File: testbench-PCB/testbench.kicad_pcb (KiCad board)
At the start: 2 copper layers, 185.4 x 134.6 mm, 67 parts, among them J1 USB_C_Receptacle_USB2.0, J2 AVR-ISP, J3 AVR-JTAG, SW1 SW_Push, U1 ATmega2561-16A, U10 CH340C, U2 Thermistor_module, U3 Rotary_encoder_switch_module, U4 RTC_EEPROM_module, U6 Relay_module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

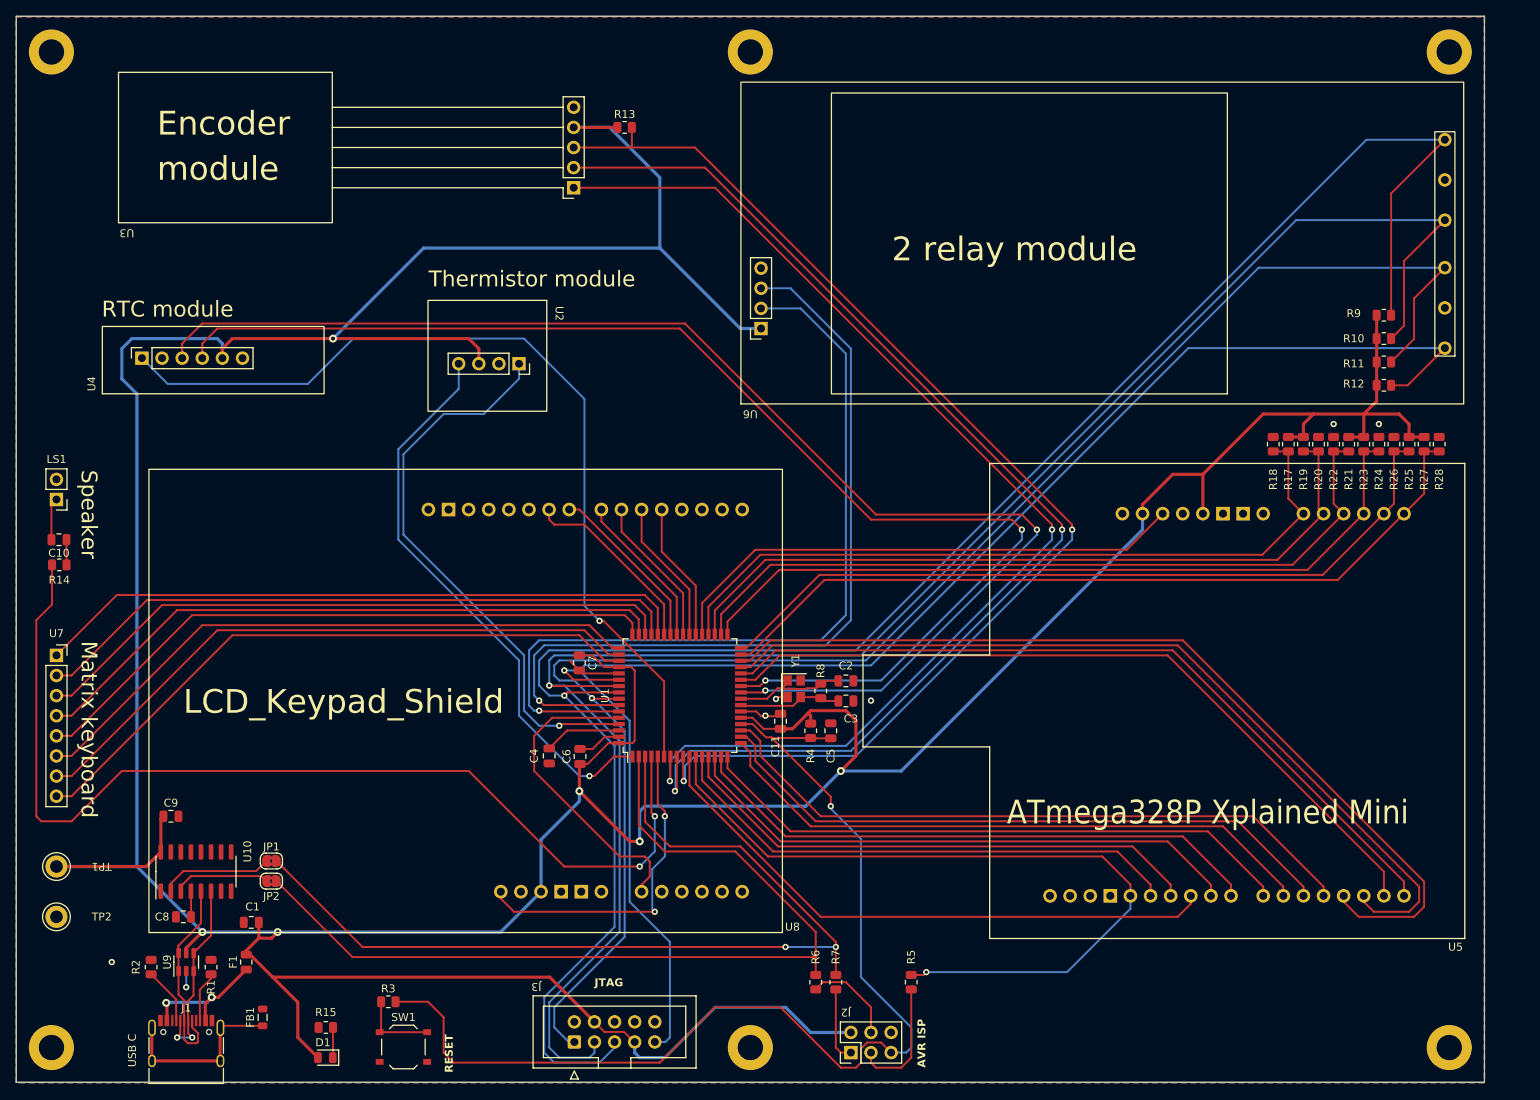
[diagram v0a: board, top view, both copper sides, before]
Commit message: Changed encoder module pinout, added labels.
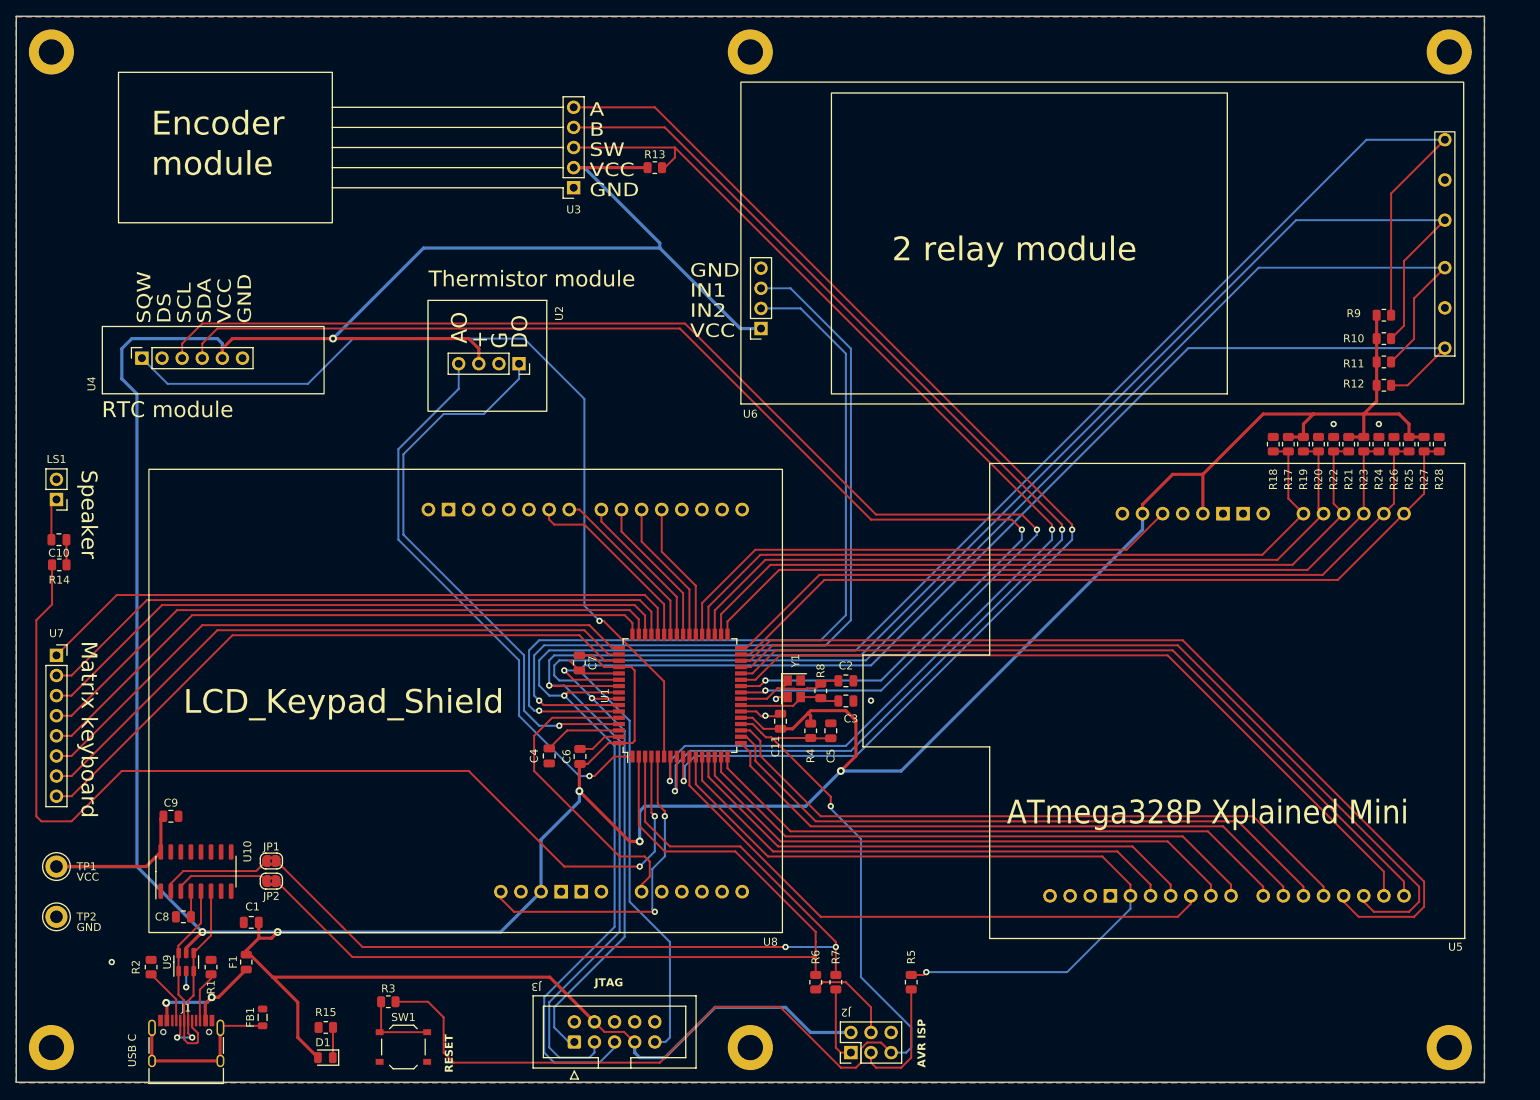
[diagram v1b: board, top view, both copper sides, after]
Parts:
- moved R13 6.35 mm to (118.7, 46.4)
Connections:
- U1 pad 7: /Kit modules/ENC.A -> /Kit modules/ENC.SW
- U1 pad 9: /Kit modules/ENC.SW -> /Kit modules/ENC.A
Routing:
- net /Kit modules/ENC.A: track 145.4 -> 152.5 mm
- net +5V: track 638.7 -> 635.6 mm
- net /Kit modules/ENC.B: track 150.6 -> 152.7 mm
- net /Kit modules/ENC.SW: track 153.1 -> 151.0 mm
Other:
- board text added: "+"
- board text added: "A"
- board text added: "AO"
- board text added: "B"
- board text added: "DO"
- board text added: "DS"
- board text added: "G"
- board text added: "GND"
- board text added: "IN1"
- board text added: "IN2"
- board text added: "SCL"
- board text added: "SDA"
- board text added: "SQW"
- board text added: "SW"
- board text added: "VCC"

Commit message: Added protective resistors.
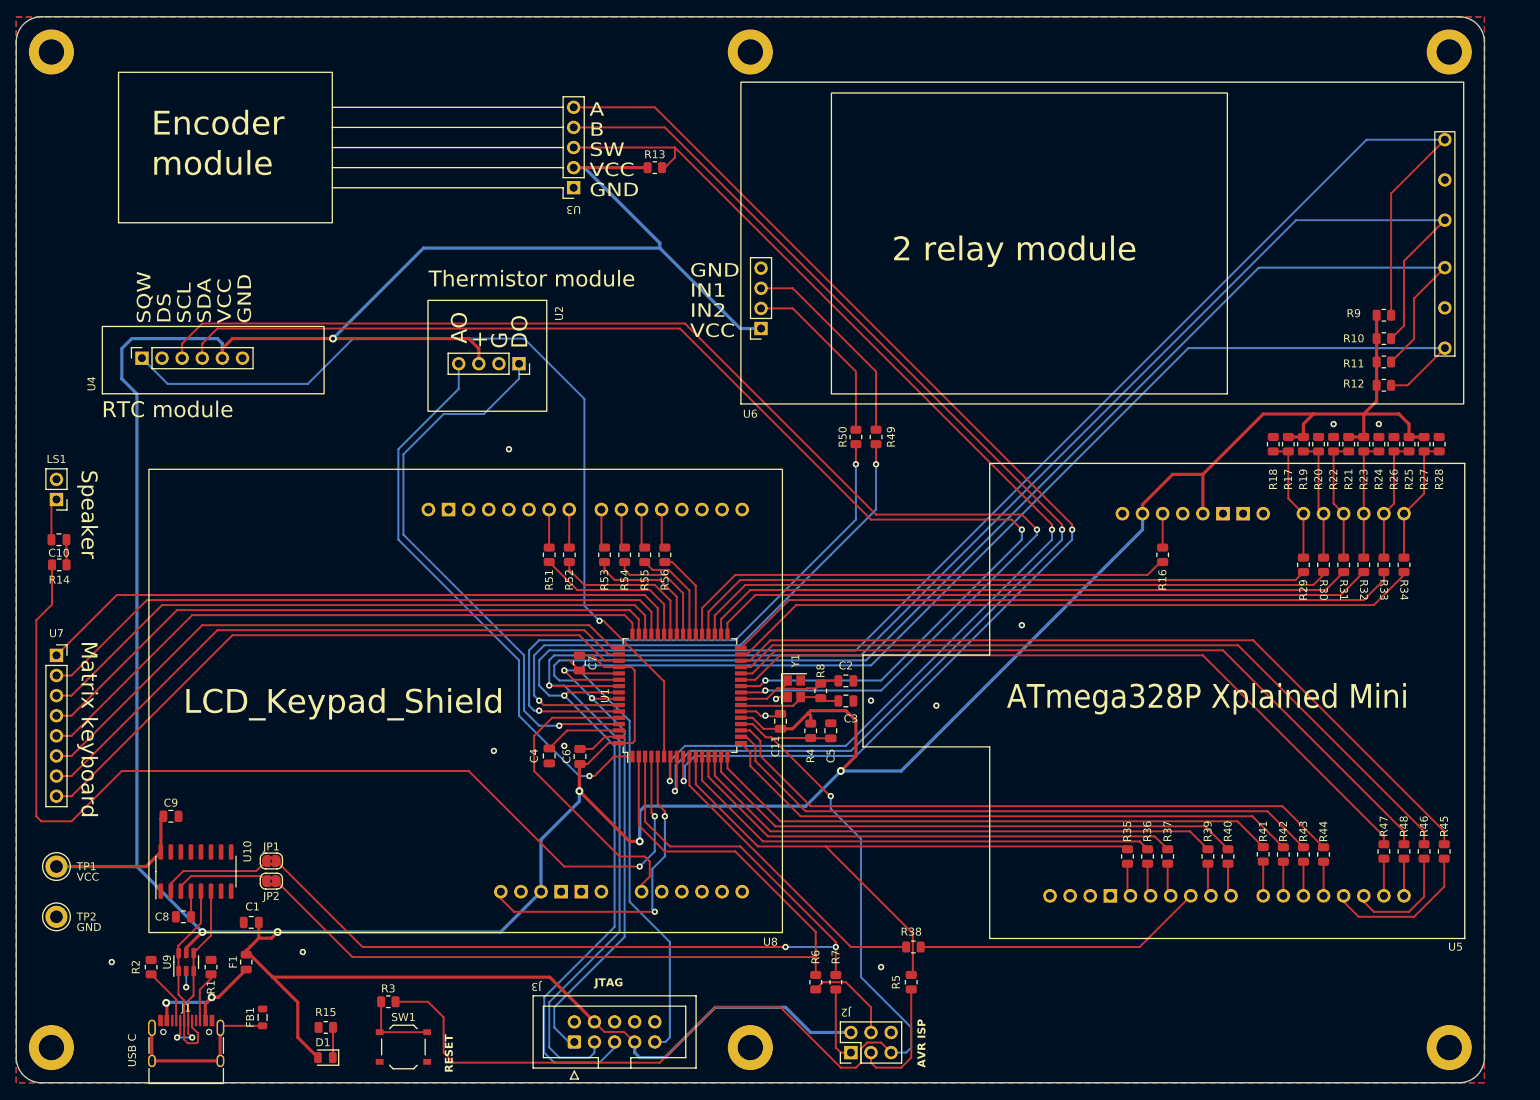
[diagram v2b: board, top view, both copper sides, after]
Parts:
- added R16: 330R, Resistor_SMD:R_0805_2012Metric, F.Cu at (182.9, 95.2)
- added R29: 330R, Resistor_SMD:R_0805_2012Metric, F.Cu at (200.7, 96.5)
- added R30: 330R, Resistor_SMD:R_0805_2012Metric, F.Cu at (203.2, 96.5)
- added R31: 330R, Resistor_SMD:R_0805_2012Metric, F.Cu at (205.7, 96.5)
- added R32: 330R, Resistor_SMD:R_0805_2012Metric, F.Cu at (208.3, 96.5)
- added R33: 330R, Resistor_SMD:R_0805_2012Metric, F.Cu at (210.8, 96.5)
- added R34: 330R, Resistor_SMD:R_0805_2012Metric, F.Cu at (213.4, 96.5)
- added R35: 330R, Resistor_SMD:R_0805_2012Metric, F.Cu at (178.4, 133.3)
- added R36: 330R, Resistor_SMD:R_0805_2012Metric, F.Cu at (181.0, 133.3)
- added R37: 330R, Resistor_SMD:R_0805_2012Metric, F.Cu at (183.5, 133.3)
- added R38: 330R, Resistor_SMD:R_0805_2012Metric, F.Cu at (151.4, 144.8)
- added R39: 330R, Resistor_SMD:R_0805_2012Metric, F.Cu at (188.6, 133.3)
- added R40: 330R, Resistor_SMD:R_0805_2012Metric, F.Cu at (191.1, 133.3)
- added R41: 330R, Resistor_SMD:R_0805_2012Metric, F.Cu at (195.6, 133.1)
- added R42: 330R, Resistor_SMD:R_0805_2012Metric, F.Cu at (198.1, 133.1)
- added R43: 330R, Resistor_SMD:R_0805_2012Metric, F.Cu at (200.7, 133.1)
- added R44: 330R, Resistor_SMD:R_0805_2012Metric, F.Cu at (203.2, 133.1)
- added R45: 330R, Resistor_SMD:R_0805_2012Metric, F.Cu at (218.4, 132.7)
- added R46: 330R, Resistor_SMD:R_0805_2012Metric, F.Cu at (215.9, 132.7)
- added R47: 330R, Resistor_SMD:R_0805_2012Metric, F.Cu at (210.8, 132.7)
- added R48: 330R, Resistor_SMD:R_0805_2012Metric, F.Cu at (213.4, 132.7)
- added R49: 330R, Resistor_SMD:R_0805_2012Metric, F.Cu at (146.7, 80.4)
- added R50: 330R, Resistor_SMD:R_0805_2012Metric, F.Cu at (144.1, 80.4)
- added R51: 330R, Resistor_SMD:R_0805_2012Metric, F.Cu at (105.4, 95.2)
- added R52: 330R, Resistor_SMD:R_0805_2012Metric, F.Cu at (108.0, 95.2)
- added R53: 330R, Resistor_SMD:R_0805_2012Metric, F.Cu at (112.4, 95.2)
- added R54: 330R, Resistor_SMD:R_0805_2012Metric, F.Cu at (114.9, 95.2)
- added R55: 330R, Resistor_SMD:R_0805_2012Metric, F.Cu at (117.5, 95.2)
- added R56: 330R, Resistor_SMD:R_0805_2012Metric, F.Cu at (120.0, 95.2)
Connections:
- R17 pad 2: /ATmega328P module/DUT_D1 -> /ATmega328P module/D1
- R18 pad 1: /ATmega328P module/DUT_D1 -> /ATmega328P module/D1
- R19 pad 2: /ATmega328P module/DUT_D2 -> /ATmega328P module/D2
- R20 pad 1: /ATmega328P module/DUT_D2 -> /ATmega328P module/D2
- R21 pad 2: /ATmega328P module/DUT_D3 -> /ATmega328P module/D3
- R22 pad 1: /ATmega328P module/DUT_D3 -> /ATmega328P module/D3
- R23 pad 2: /ATmega328P module/DUT_D4 -> /ATmega328P module/D4
- R24 pad 1: /ATmega328P module/DUT_D4 -> /ATmega328P module/D4
- R25 pad 2: /ATmega328P module/DUT_D5 -> /ATmega328P module/D5
- R26 pad 1: /ATmega328P module/DUT_D5 -> /ATmega328P module/D5
- R27 pad 2: /ATmega328P module/DUT_D6 -> /ATmega328P module/D6
- R28 pad 1: /ATmega328P module/DUT_D6 -> /ATmega328P module/D6
- U5 pad 1: /ATmega328P module/DUT_D7 -> /ATmega328P module/D20
- U5 pad 10: /ATmega328P module/DUT_D16 -> /ATmega328P module/D11
- U5 pad 11: /ATmega328P module/DUT_D17 -> /ATmega328P module/D10
- U5 pad 12: /ATmega328P module/DUT_D18 -> /ATmega328P module/D9
- U5 pad 13: /ATmega328P module/DUT_D19 -> /ATmega328P module/D8
- U5 pad 14: /ATmega328P module/DUT_D20 -> /ATmega328P module/D7
- U5 pad 2: /ATmega328P module/DUT_D8 -> /ATmega328P module/D19
- U5 pad 21: /ATmega328P module/DUT_D0 -> /ATmega328P module/D0
- U5 pad 27: /ATmega328P module/DUT_D1 -> /ATmega328P module/D1
- U5 pad 28: /ATmega328P module/DUT_D2 -> /ATmega328P module/D2
- U5 pad 29: /ATmega328P module/DUT_D3 -> /ATmega328P module/D3
- U5 pad 3: /ATmega328P module/DUT_D9 -> /ATmega328P module/D18
- U5 pad 30: /ATmega328P module/DUT_D4 -> /ATmega328P module/D4
- U5 pad 31: /ATmega328P module/DUT_D5 -> /ATmega328P module/D5
- U5 pad 32: /ATmega328P module/DUT_D6 -> /ATmega328P module/D6
- U5 pad 4: /ATmega328P module/DUT_D10 -> /ATmega328P module/D17
- U5 pad 5: /ATmega328P module/DUT_D11 -> /ATmega328P module/D16
- U5 pad 6: /ATmega328P module/DUT_D12 -> /ATmega328P module/D15
- U5 pad 7: /ATmega328P module/DUT_D13 -> /ATmega328P module/D14
- U5 pad 8: /ATmega328P module/DUT_D14 -> /ATmega328P module/D13
- U5 pad 9: /ATmega328P module/DUT_D15 -> /ATmega328P module/D12
- U6 pad 2: /Kit modules/K1-IN -> Net-(U6-IN1)
- U6 pad 3: /Kit modules/K2-IN -> Net-(U6-IN2)
- U8 pad 10: /Kit modules/LCD_D5 -> Net-(U8-E)
- U8 pad 5: /Kit modules/LCD_D0 -> Net-(U8-D4)
- U8 pad 6: /Kit modules/LCD_D1 -> Net-(U8-D5)
- U8 pad 7: /Kit modules/LCD_D2 -> Net-(U8-D6)
- U8 pad 8: /Kit modules/LCD_D3 -> Net-(U8-D7)
- U8 pad 9: /Kit modules/LCD_D4 -> Net-(U8-RS)
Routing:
- net /ATmega328P module/D10: track 0.00 -> 36.8 mm
- net /ATmega328P module/DUT_D17: track 75.5 -> 39.5 mm
- net /Kit modules/K1-IN: track 106.9 -> 75.4 mm, vias 1 -> 2
- net /Kit modules/K2-IN: track 106.6 -> 76.3 mm, vias 1 -> 2
- net Net-(U6-IN1): track 0.00 -> 26.2 mm
- net Net-(U6-IN2): track 0.00 -> 22.6 mm
- net /ATmega328P module/D17: track 0.00 -> 18.6 mm
- net /ATmega328P module/D6: track 0.00 -> 16.4 mm
- net /ATmega328P module/D1: track 0.00 -> 16.1 mm
- net /ATmega328P module/D3: track 0.00 -> 15.8 mm
- net /ATmega328P module/D5: track 0.00 -> 15.8 mm
- net /ATmega328P module/D2: track 0.00 -> 15.6 mm
- net /ATmega328P module/DUT_D20: track 97.8 -> 82.3 mm, vias 1 -> 0
- net /ATmega328P module/D4: track 0.00 -> 15.3 mm
- net /ATmega328P module/D18: track 0.00 -> 14.5 mm
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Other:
- outline, holes or cut-outs redrawn
- board text added: "Author: Ivo Zaludek"
- board text added: "Rev.: v0.1"
- board text added: "Test bench for MPC-POR educational kit"
- board text added: "VUT Brno, 2023"

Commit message: Added logo and label. Rearanged labels.
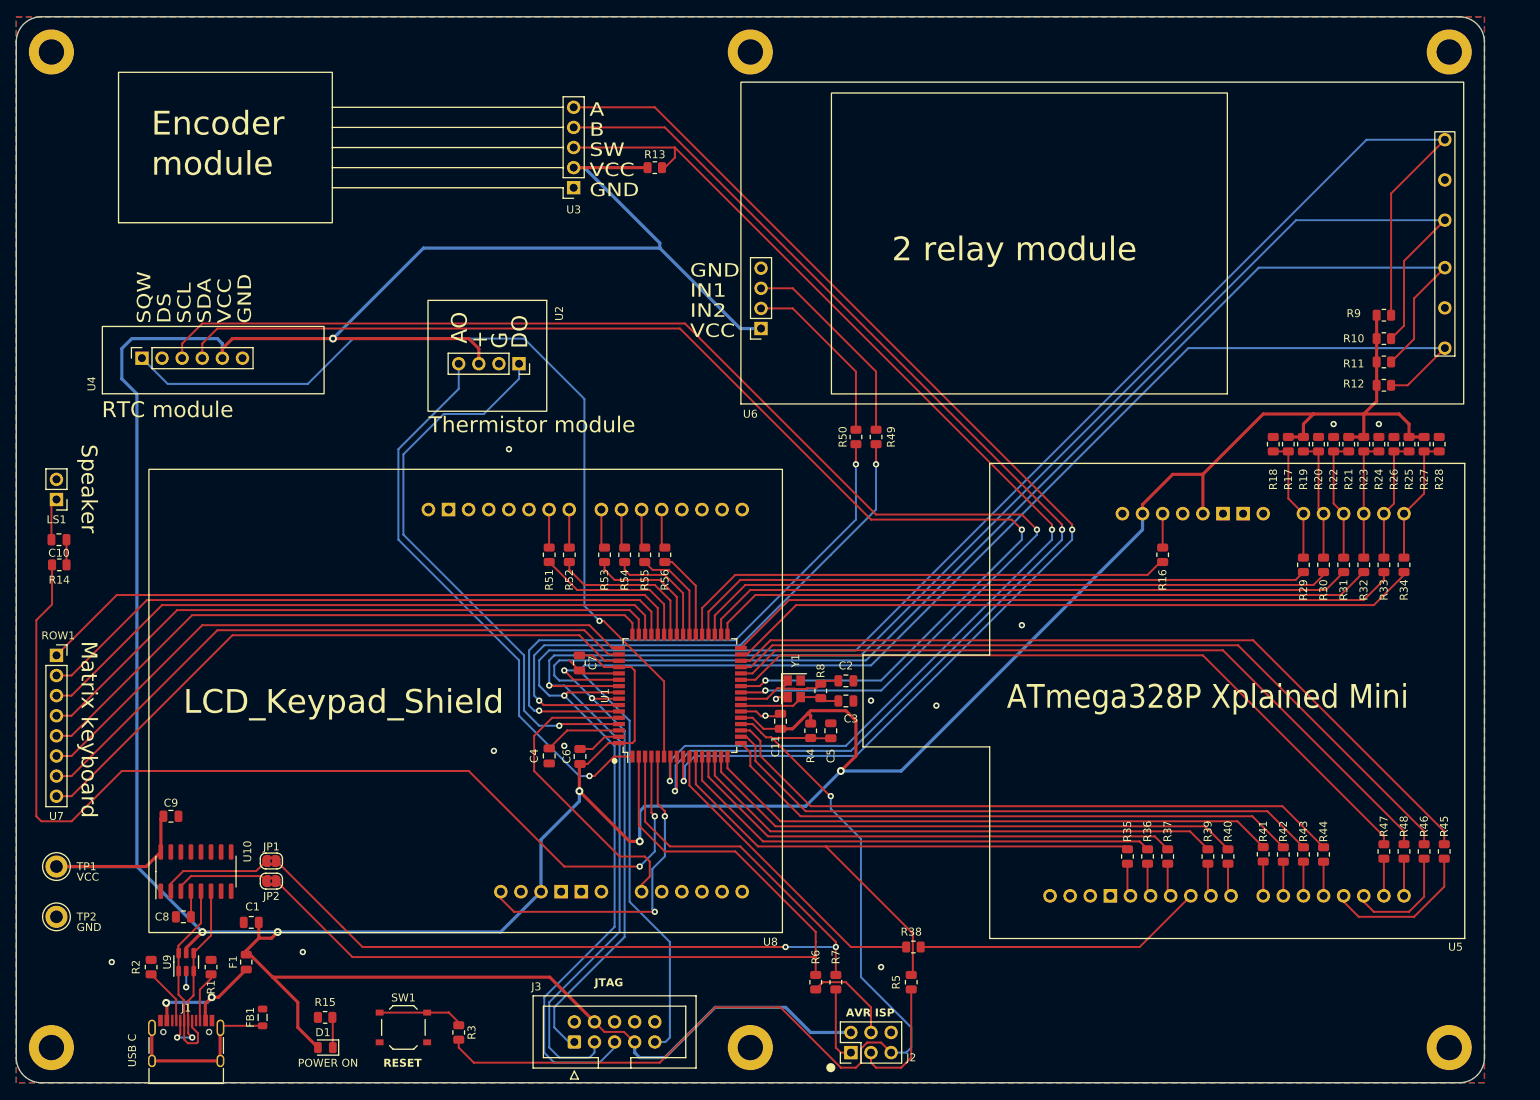
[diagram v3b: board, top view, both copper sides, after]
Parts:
- added G***: LOGO, LOGO, B.Cu at (198.1, 45.7)
- moved R3 9.70 mm to (94.0, 155.6), turned to -90 degrees
- moved SW1 2.47 mm to (87.0, 154.9)
- moved R15 1.27 mm to (77.1, 153.7)
- moved D1 1.27 mm to (77.1, 157.5)
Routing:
- net /MCU/RST: track 138.7 -> 126.7 mm
- net +5V: track 635.6 -> 634.3 mm
- net Net-(R3-Pad1): track 9.92 -> 10.9 mm
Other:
- board text added: "POWER ON"
- board text added: "ROW1"
